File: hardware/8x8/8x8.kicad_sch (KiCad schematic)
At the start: 11 parts

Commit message: Updated Pin Headers
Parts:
- removed Pin_Header_1, Pin_Header_2: Conn_01x16_Male, symbol Connector:Conn_01x16_Male
- added Pin_Header_1: Conn_02x16_Odd_Even, Connector_PinHeader_2.54mm:PinHeader_2x16_P2.54mm_Vertical, symbol Connector_Generic:Conn_02x16_Odd_Even
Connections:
- net +3V3: now also Pin_Header_1.7 (Pin_7), Pin_Header_1.8 (Pin_8)
- net +5V: now also Pin_Header_1.10 (Pin_10), Pin_Header_1.9 (Pin_9)
- net +9V: now also Pin_Header_1.11 (Pin_11), Pin_Header_1.12 (Pin_12)
- net GND: now also Pin_Header_1.1 (Pin_1), Pin_Header_1.2 (Pin_2), Pin_Header_1.3 (Pin_3), Pin_Header_1.4 (Pin_4), Pin_Header_1.5 (Pin_5), Pin_Header_1.6 (Pin_6)
- net I2C_SCL: now also Pin_Header_1.27 (Pin_27), Pin_Header_1.28 (Pin_28)
- net I2C_SDA_3V3: now also Pin_Header_1.29 (Pin_29), Pin_Header_1.30 (Pin_30)
- net I2C_SDA_5V: now also Pin_Header_1.31 (Pin_31), Pin_Header_1.32 (Pin_32)
- net SPI_MISO_3V3: now also Pin_Header_1.23 (Pin_23), Pin_Header_1.24 (Pin_24)
- net SPI_MISO_5V: now also Pin_Header_1.25 (Pin_25), Pin_Header_1.26 (Pin_26)
- net SPI_MOSI: now also Pin_Header_1.21 (Pin_21), Pin_Header_1.22 (Pin_22)
- net SPI_SCK: now also Pin_Header_1.19 (Pin_19), Pin_Header_1.20 (Pin_20)
- net SPI_SS_0: now also Pin_Header_1.17 (Pin_17), Pin_Header_1.18 (Pin_18)
- net SPI_SS_1: now also Pin_Header_1.15 (Pin_15), Pin_Header_1.16 (Pin_16)
- net SPI_SS_2: now also Pin_Header_1.13 (Pin_13), Pin_Header_1.14 (Pin_14)

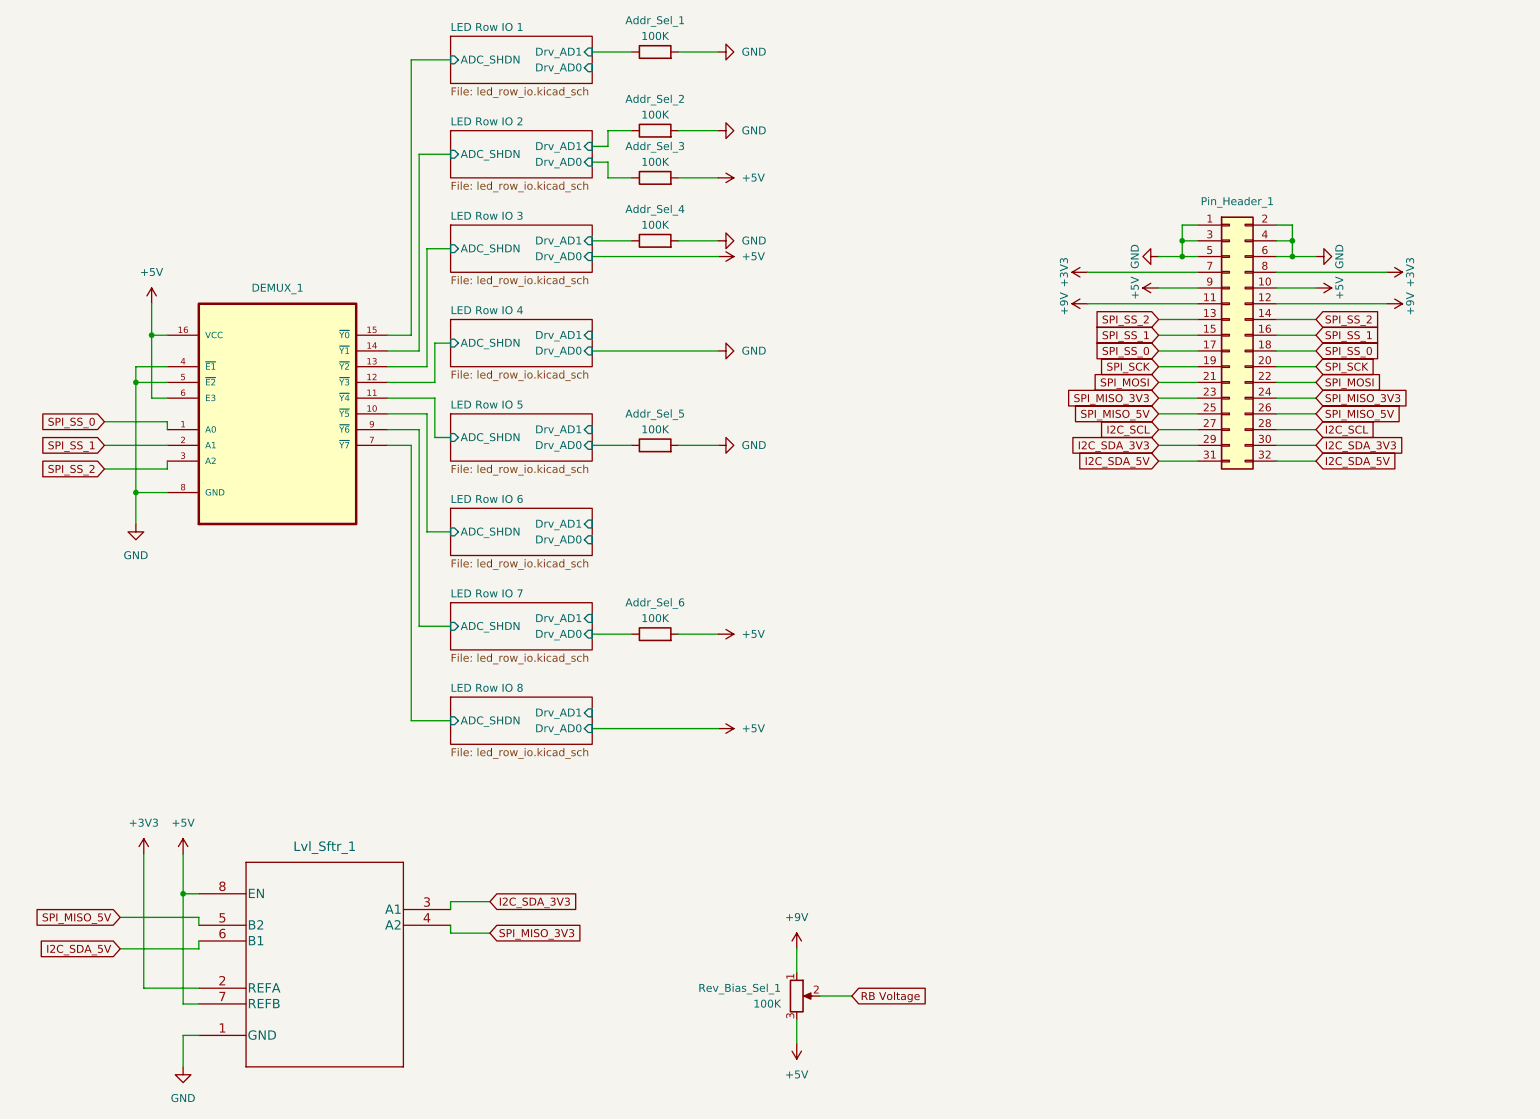
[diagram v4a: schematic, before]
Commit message: Updated Footprints
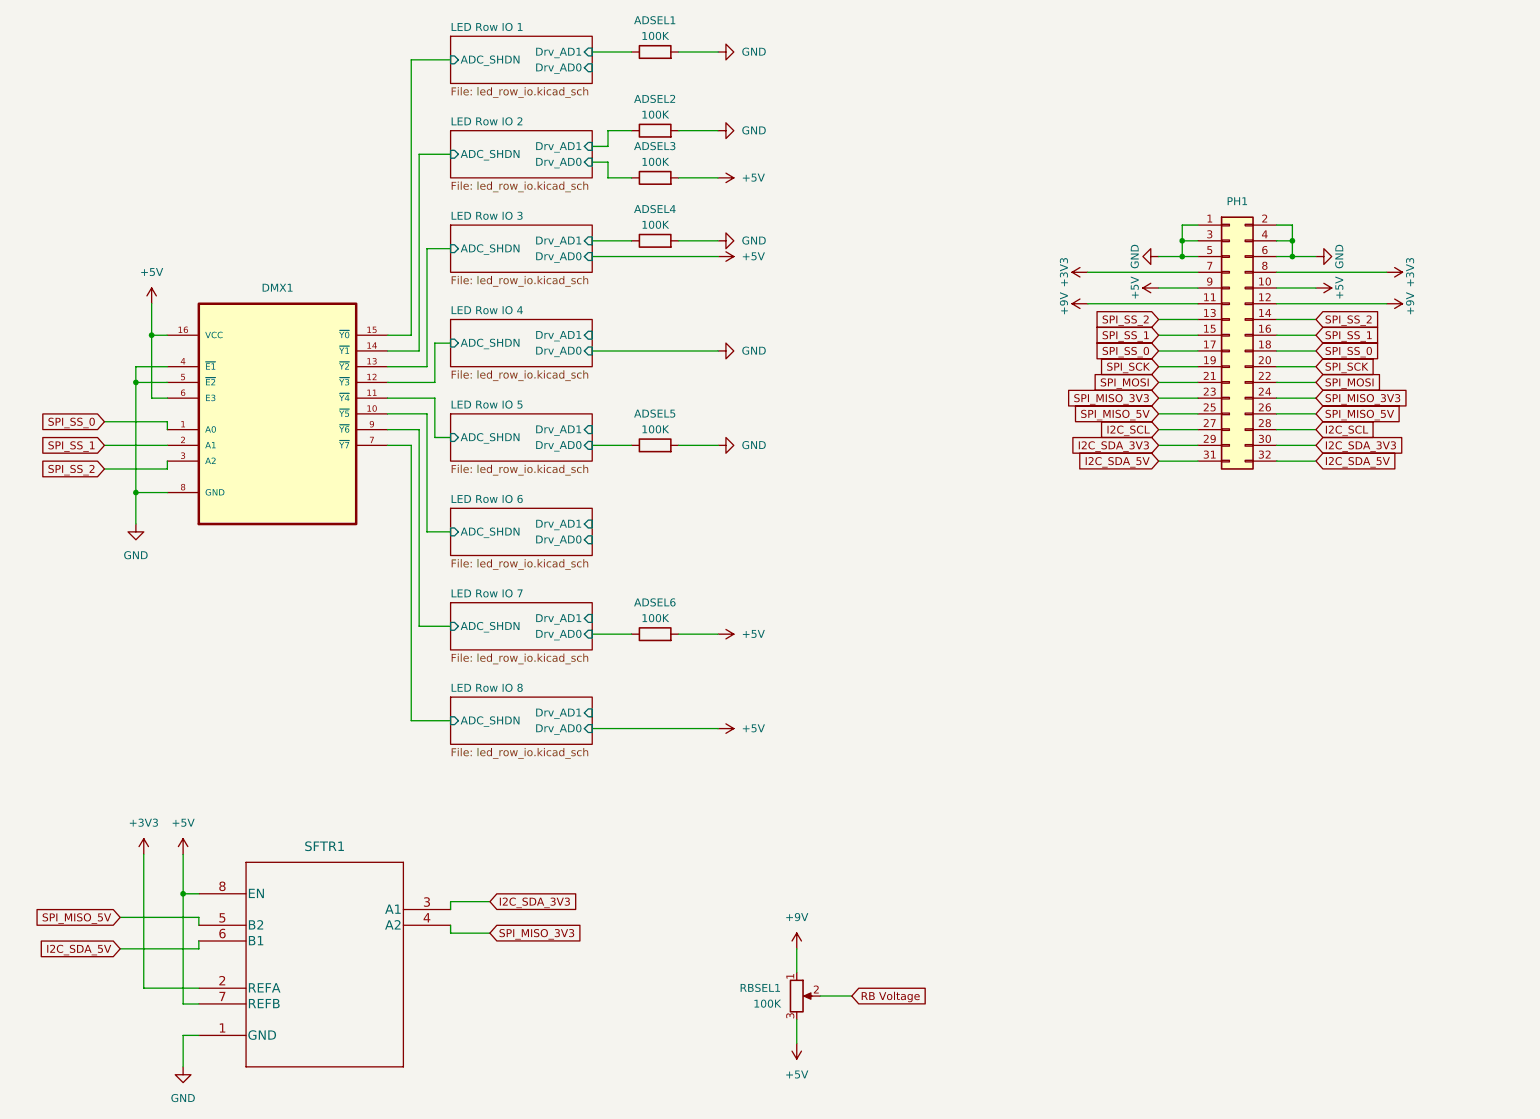
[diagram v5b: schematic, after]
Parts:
- ADSEL1: renamed from Addr_Sel_1; footprint Resistor_THT:R_Axial_DIN0207_L6.3mm_D2.5mm_P7.62mm_Horizontal -> Resistor TH:footprints
- ADSEL2: renamed from Addr_Sel_2; footprint Resistor_THT:R_Axial_DIN0207_L6.3mm_D2.5mm_P7.62mm_Horizontal -> Resistor TH:footprints
- ADSEL3: renamed from Addr_Sel_3; footprint Resistor_THT:R_Axial_DIN0207_L6.3mm_D2.5mm_P7.62mm_Horizontal -> Resistor TH:footprints
- ADSEL4: renamed from Addr_Sel_4; footprint Resistor_THT:R_Axial_DIN0207_L6.3mm_D2.5mm_P7.62mm_Horizontal -> Resistor TH:footprints
- ADSEL5: renamed from Addr_Sel_5; footprint Resistor_THT:R_Axial_DIN0207_L6.3mm_D2.5mm_P7.62mm_Horizontal -> Resistor TH:footprints
- ADSEL6: renamed from Addr_Sel_6; footprint Resistor_THT:R_Axial_DIN0207_L6.3mm_D2.5mm_P7.62mm_Horizontal -> Resistor TH:footprints
- renumbered DEMUX_1 to DMX1, Pin_Header_1 to PH1, Rev_Bias_Sel_1 to RBSEL1, Lvl_Sftr_1 to SFTR1

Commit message: Completed Major Routing
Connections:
- net LED Row IO 3/ADC_SHDN renamed LED 4x2 Left 2/ADC_SHDN
- net LED Row IO 3/Drv_AD1 renamed LED 4x2 Left 2/Drv_AD1
- net LED Row IO 4/ADC_SHDN renamed LED 4x2 Right 2/ADC_SHDN
- net LED Row IO 5/ADC_SHDN renamed LED 4x2 Left 3/ADC_SHDN
- net LED Row IO 5/Drv_AD0 renamed LED 4x2 Left 3/Drv_AD0
- net LED Row IO 6/ADC_SHDN renamed LED 4x2 Right 3/ADC_SHDN
- net LED Row IO 7/ADC_SHDN renamed LED 4x2 Left 4/ADC_SHDN
- net LED Row IO 7/Drv_AD0 renamed LED 4x2 Left 4/Drv_AD0
- net LED Row IO 8/ADC_SHDN renamed LED 4x2 Right 4/ADC_SHDN
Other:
- sheet LED Row IO 1 renamed LED 4x2 Left 1
- sheet LED Row IO 2 renamed LED 4x2 Right 1
- removed sheet LED Row IO 3
- removed sheet LED Row IO 4
- removed sheet LED Row IO 5
- removed sheet LED Row IO 6
- removed sheet LED Row IO 7
- removed sheet LED Row IO 8
- added sheet LED 4x2 Left 2 (led_4x2_left.kicad_sch)
- added sheet LED 4x2 Left 3 (led_4x2_left.kicad_sch)
- added sheet LED 4x2 Left 4 (led_4x2_left.kicad_sch)
- added sheet LED 4x2 Right 2 (led_4x2_right.kicad_sch)
- added sheet LED 4x2 Right 3 (led_4x2_right.kicad_sch)
- added sheet LED 4x2 Right 4 (led_4x2_right.kicad_sch)
- sheet LED 4x2 Left 1: file led_row_io.kicad_sch -> led_4x2_left.kicad_sch
- sheet LED 4x2 Right 1: file led_row_io.kicad_sch -> led_4x2_right.kicad_sch

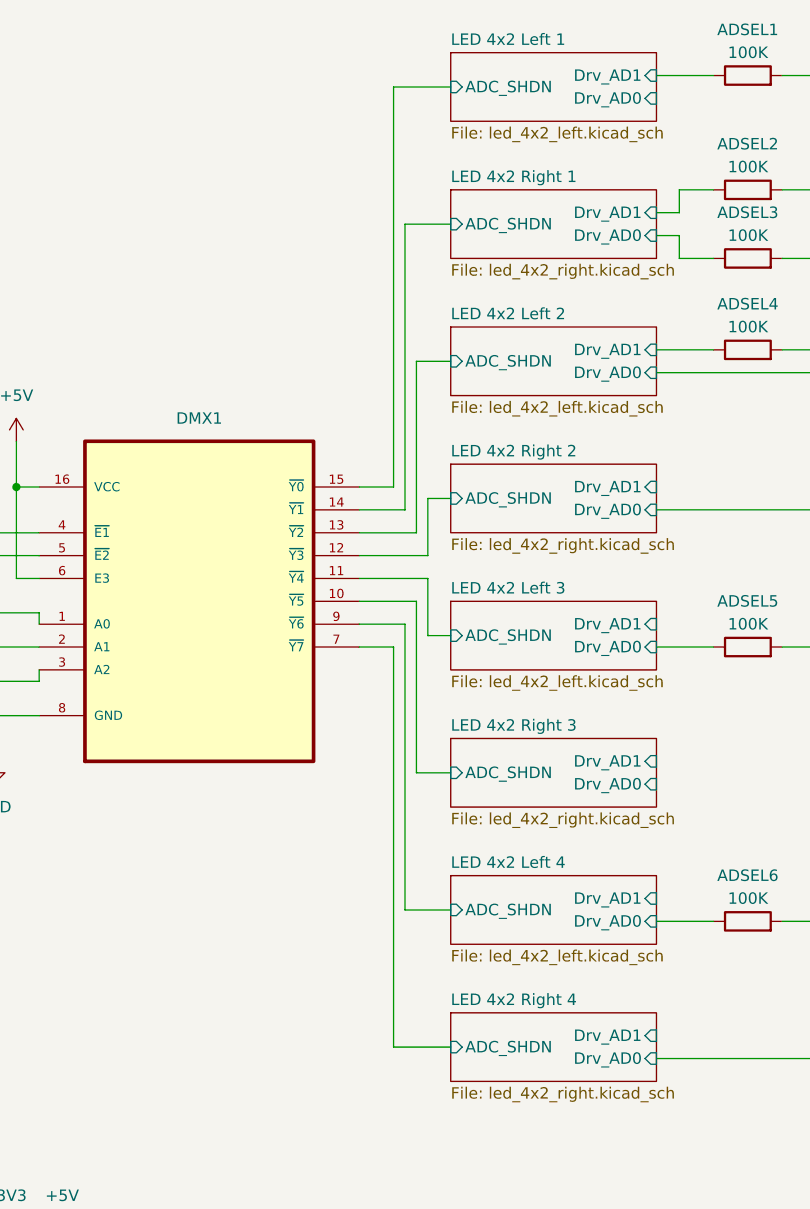
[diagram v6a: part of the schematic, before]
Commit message: Completed 8x8 Routing
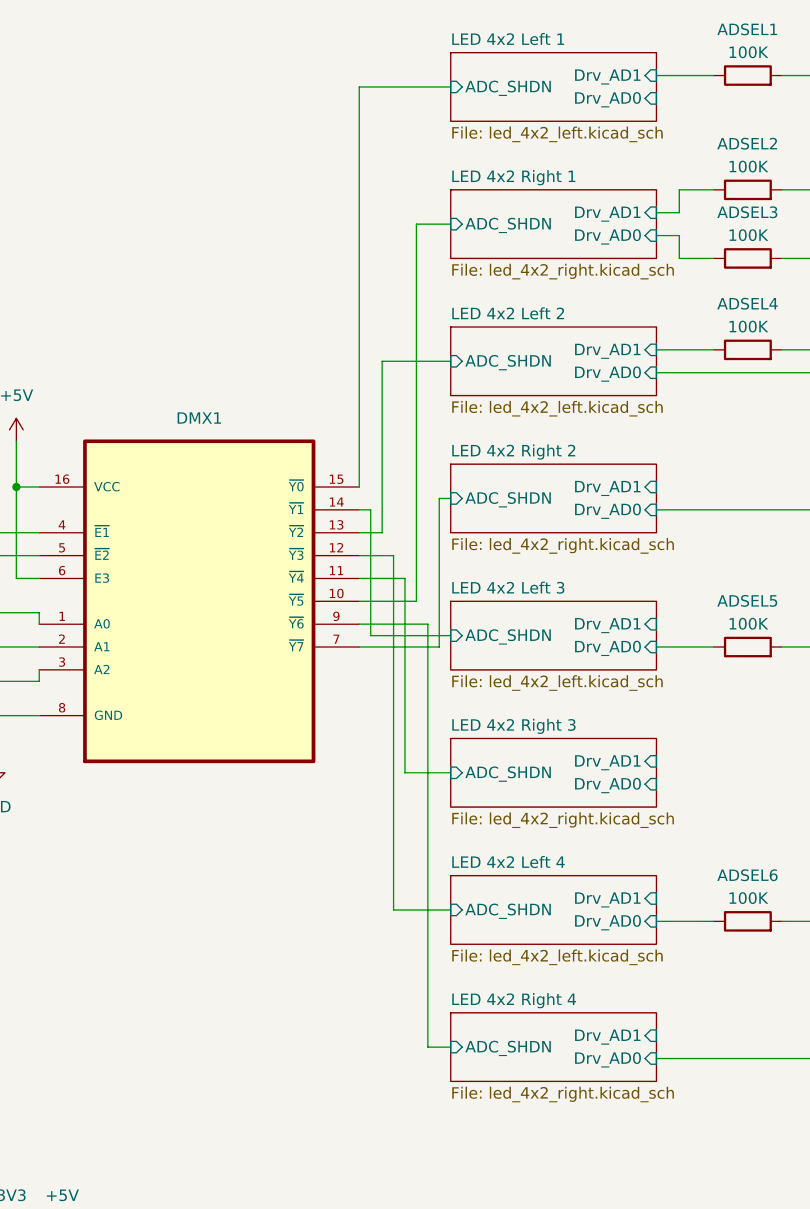
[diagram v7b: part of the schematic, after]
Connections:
- net LED 4x2 Left 3/ADC_SHDN: now also DMX1.14 (~{Y1}); no longer DMX1.11 (~{Y4})
- net LED 4x2 Left 4/ADC_SHDN: now also DMX1.12 (~{Y3}); no longer DMX1.9 (~{Y6})
- net LED 4x2 Right 1/ADC_SHDN: now also DMX1.10 (~{Y5}); no longer DMX1.14 (~{Y1})
- net LED 4x2 Right 2/ADC_SHDN: now also DMX1.7 (~{Y7}); no longer DMX1.12 (~{Y3})
- net LED 4x2 Right 3/ADC_SHDN: now also DMX1.11 (~{Y4}); no longer DMX1.10 (~{Y5})
- net LED 4x2 Right 4/ADC_SHDN: now also DMX1.9 (~{Y6}); no longer DMX1.7 (~{Y7})
